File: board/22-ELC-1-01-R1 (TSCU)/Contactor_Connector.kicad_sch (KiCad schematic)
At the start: 18 parts, among them J10 Conn_02x02_Counter_Clockwise, J9 Conn_02x02_Counter_Clockwise, Q12 2N7002, Q13 CSD18540Q5B

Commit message: Ready for review
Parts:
- renumbered C27 to C6, C28 to C7, D8 to D5, J9 to J8, J10 to J9, Q12 to Q2, Q13 to Q3, R47 to R10, R48 to R11, R49 to R12, R50 to R13, R51 to R14, R43 to R7, R46 to R8, R36 to R9, TP15 to TP7, TP16 to TP8, TP17 to TP9
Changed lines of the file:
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@@
   (symbol (lib_id "power:GND") (at 74.93 120.65 0) (unit 1)
     (in_bom yes) (on_board yes)
-    (property "Reference" "#PWR093" (id 0) (at 74.93 127 0)
+    (property "Reference" "#PWR030" (id 0) (at 74.93 127 0)
       (effects (font (size 1.27 1.27)) hide)
     )
@@
   (symbol (lib_id "Device:R") (at 59.69 113.03 90) (unit 1)
     (in_bom yes) (on_board yes)
-    (property "Reference" "R43" (id 0) (at 58.5216 111.252 0)
+    (property "Reference" "R7" (id 0) (at 58.5216 111.252 0)
       (effects (font (size 1.27 1.27)) (justify left))
     )
@@
   (symbol (lib_id "Device:R") (at 80.01 106.68 270) (unit 1)
     (in_bom yes) (on_board yes)
-    (property "Reference" "R46" (id 0) (at 80.01 101.4222 90))
+    (property "Reference" "R8" (id 0) (at 80.01 101.4222 90))
     (property "Value" "100" (id 1) (at 80.01 103.7336 90))
     (property "Footprint" "Resistor_SMD:R_0603_1608Metric_Pad0.98x0.95mm_HandSolder" (id 2) (at 80.01 104.902 90)
@@
   (symbol (lib_id "Device:Q_NMOS_GSD") (at 72.39 113.03 0) (unit 1)
     (in_bom yes) (on_board yes)
-    (property "Reference" "Q12" (id 0) (at 77.6224 111.8616 0)
+    (property "Reference" "Q2" (id 0) (at 77.6224 111.8616 0)
       (effects (font (size 1.27 1.27)) (justify left))
     )
@@
   (symbol (lib_id "Device:R") (at 92.71 140.97 0) (unit 1)
     (in_bom yes) (on_board yes)
-    (property "Reference" "R47" (id 0) (at 94.488 139.8016 0)
+    (property "Reference" "R10" (id 0) (at 94.488 139.8016 0)
       (effects (font (size 1.27 1.27)) (justify left))
     )
@@
   (symbol (lib_id "Device:LED") (at 92.71 151.13 90) (unit 1)
     (in_bom yes) (on_board yes)
-    (property "Reference" "D8" (id 0) (at 95.7072 150.1394 90)
+    (property "Reference" "D5" (id 0) (at 95.7072 150.1394 90)
       (effects (font (size 1.27 1.27)) (justify right))
     )
@@
   (symbol (lib_id "power:GND") (at 92.71 154.94 0) (unit 1)
     (in_bom yes) (on_board yes)
-    (property "Reference" "#PWR094" (id 0) (at 92.71 161.29 0)
+    (property "Reference" "#PWR032" (id 0) (at 92.71 161.29 0)
       (effects (font (size 1.27 1.27)) hide)
     )
@@
   (symbol (lib_id "Device:R") (at 241.3 93.98 270) (unit 1)
     (in_bom yes) (on_board yes)
-    (property "Reference" "R51" (id 0) (at 241.3 88.7222 90))
+    (property "Reference" "R14" (id 0) (at 241.3 88.7222 90))
     (property "Value" "1k" (id 1) (at 241.3 91.0336 90))
     (property "Footprint" "Resistor_SMD:R_0603_1608Metric_Pad0.98x0.95mm_HandSolder" (id 2) (at 241.3 92.202 90)
@@
   (symbol (lib_id "power:+5V") (at 208.28 97.79 180) (unit 1)
     (in_bom yes) (on_board yes)
-    (property "Reference" "#PWR097" (id 0) (at 208.28 93.98 0)
+    (property "Reference" "#PWR035" (id 0) (at 208.28 93.98 0)
       (effects (font (size 1.27 1.27)) hide)
     )
@@
   (symbol (lib_id "power:+5V") (at 128.905 96.52 0) (unit 1)
     (in_bom yes) (on_board yes)
-    (property "Reference" "#PWR095" (id 0) (at 128.905 100.33 0)
+    (property "Reference" "#PWR033" (id 0) (at 128.905 100.33 0)
       (effects (font (size 1.27 1.27)) hide)
     )
@@
   (symbol (lib_id "Connector_Generic:Conn_02x02_Counter_Clockwise") (at 151.13 83.82 0) (unit 1)
     (in_bom yes) (on_board yes)
-    (property "Reference" "J9" (id 0) (at 152.4 81.28 0))
+    (property "Reference" "J8" (id 0) (at 152.4 81.28 0))
     (property "Value" "Conn_02x02_Counter_Clockwise" (id 1) (at 152.4 74.93 0)
       (effects (font (size 1.27 1.27)) hide)
@@
   (symbol (lib_id "Connector_Generic:Conn_02x02_Counter_Clockwise") (at 217.17 83.82 0) (unit 1)
     (in_bom yes) (on_board yes)
-    (property "Reference" "J10" (id 0) (at 218.44 81.28 0))
+    (property "Reference" "J9" (id 0) (at 218.44 81.28 0))
     (property "Value" "Conn_02x02_Counter_Clockwise" (id 1) (at 218.44 74.93 0)
       (effects (font (size 1.27 1.27)) hide)
@@
   (symbol (lib_id "Device:R") (at 234.95 97.79 0) (unit 1)
     (in_bom yes) (on_board yes)
-    (property "Reference" "R50" (id 0) (at 236.728 96.6216 0)
+    (property "Reference" "R13" (id 0) (at 236.728 96.6216 0)
       (effects (font (size 1.27 1.27)) (justify left))
     )
@@
   (symbol (lib_id "Device:R") (at 210.82 91.44 0) (unit 1)
     (in_bom yes) (on_board yes)
-    (property "Reference" "R49" (id 0) (at 212.598 90.2716 0)
+    (property "Reference" "R12" (id 0) (at 212.598 90.2716 0)
       (effects (font (size 1.27 1.27)) (justify left))
     )
@@
   (symbol (lib_id "power:GND") (at 146.05 83.82 270) (unit 1)
     (in_bom yes) (on_board yes)
-    (property "Reference" "#PWR096" (id 0) (at 139.7 83.82 0)
+    (property "Reference" "#PWR034" (id 0) (at 139.7 83.82 0)
       (effects (font (size 1.27 1.27)) hide)
     )
@@
   (symbol (lib_id "power:GND") (at 212.09 83.82 270) (unit 1)
     (in_bom yes) (on_board yes)
-    (property "Reference" "#PWR098" (id 0) (at 205.74 83.82 0)
+    (property "Reference" "#PWR036" (id 0) (at 205.74 83.82 0)
       (effects (font (size 1.27 1.27)) hide)
     )
@@
   (symbol (lib_id "Device:C_Small") (at 205.74 91.44 0) (mirror y) (unit 1)
     (in_bom yes) (on_board yes)
-    (property "Reference" "C28" (id 0) (at 200.66 90.17 0)
+    (property "Reference" "C7" (id 0) (at 200.66 90.17 0)
       (effects (font (size 1.27 1.27)) (justify right))
     )
@@
   (symbol (lib_id "Device:R") (at 144.78 91.44 0) (unit 1)
     (in_bom yes) (on_board yes)
-    (property "Reference" "R48" (id 0) (at 146.558 90.2716 0)
+    (property "Reference" "R11" (id 0) (at 146.558 90.2716 0)
       (effects (font (size 1.27 1.27)) (justify left))
     )
@@
   (symbol (lib_id "Device:C_Small") (at 139.7 91.44 0) (mirror y) (unit 1)
     (in_bom yes) (on_board yes)
-    (property "Reference" "C27" (id 0) (at 134.62 90.17 0)
+    (property "Reference" "C6" (id 0) (at 134.62 90.17 0)
       (effects (font (size 1.27 1.27)) (justify right))
     )
@@
   (symbol (lib_id "LHRE_Component_Library:CSD18512Q5B") (at 227.33 93.98 0) (mirror y) (unit 1)
     (in_bom yes) (on_board yes)
-    (property "Reference" "Q13" (id 0) (at 231.14 90.17 0)
+    (property "Reference" "Q3" (id 0) (at 231.14 90.17 0)
       (effects (font (size 1.27 1.27)) (justify left))
     )
@@
   (symbol (lib_id "Connector:TestPoint") (at 62.23 57.15 0) (unit 1)
     (in_bom yes) (on_board yes)
-    (property "Reference" "TP16" (id 0) (at 60.96 52.07 0)
+    (property "Reference" "TP8" (id 0) (at 60.96 52.07 0)
       (effects (font (size 1.27 1.27)) (justify left))
     )
@@
   (symbol (lib_id "Connector:TestPoint") (at 62.23 82.55 0) (unit 1)
     (in_bom yes) (on_board yes)
-    (property "Reference" "TP17" (id 0) (at 60.96 77.47 0)
+    (property "Reference" "TP9" (id 0) (at 60.96 77.47 0)
       (effects (font (size 1.27 1.27)) (justify left))
     )
@@
   (symbol (lib_id "Connector:TestPoint") (at 53.34 113.03 0) (unit 1)
     (in_bom yes) (on_board yes)
-    (property "Reference" "TP15" (id 0) (at 52.07 107.95 0)
+    (property "Reference" "TP7" (id 0) (at 52.07 107.95 0)
       (effects (font (size 1.27 1.27)) (justify left))
     )
@@
   (symbol (lib_id "power:+5V") (at 87.63 93.98 0) (unit 1)
     (in_bom yes) (on_board yes)
-    (property "Reference" "#PWR091" (id 0) (at 87.63 97.79 0)
+    (property "Reference" "#PWR031" (id 0) (at 87.63 97.79 0)
       (effects (font (size 1.27 1.27)) hide)
     )
@@
   (symbol (lib_id "Device:R") (at 87.63 97.79 0) (unit 1)
     (in_bom yes) (on_board yes)
-    (property "Reference" "R36" (id 0) (at 89.408 96.6216 0)
-      (effects (font (size 1.27 1.27)) (justify left))
-    )
+    (property "Reference" "R9" (id 0) (at 89.408 96.6216 0)
+      (effects (font (size 1.27 1.27)) (justify left))
+    )

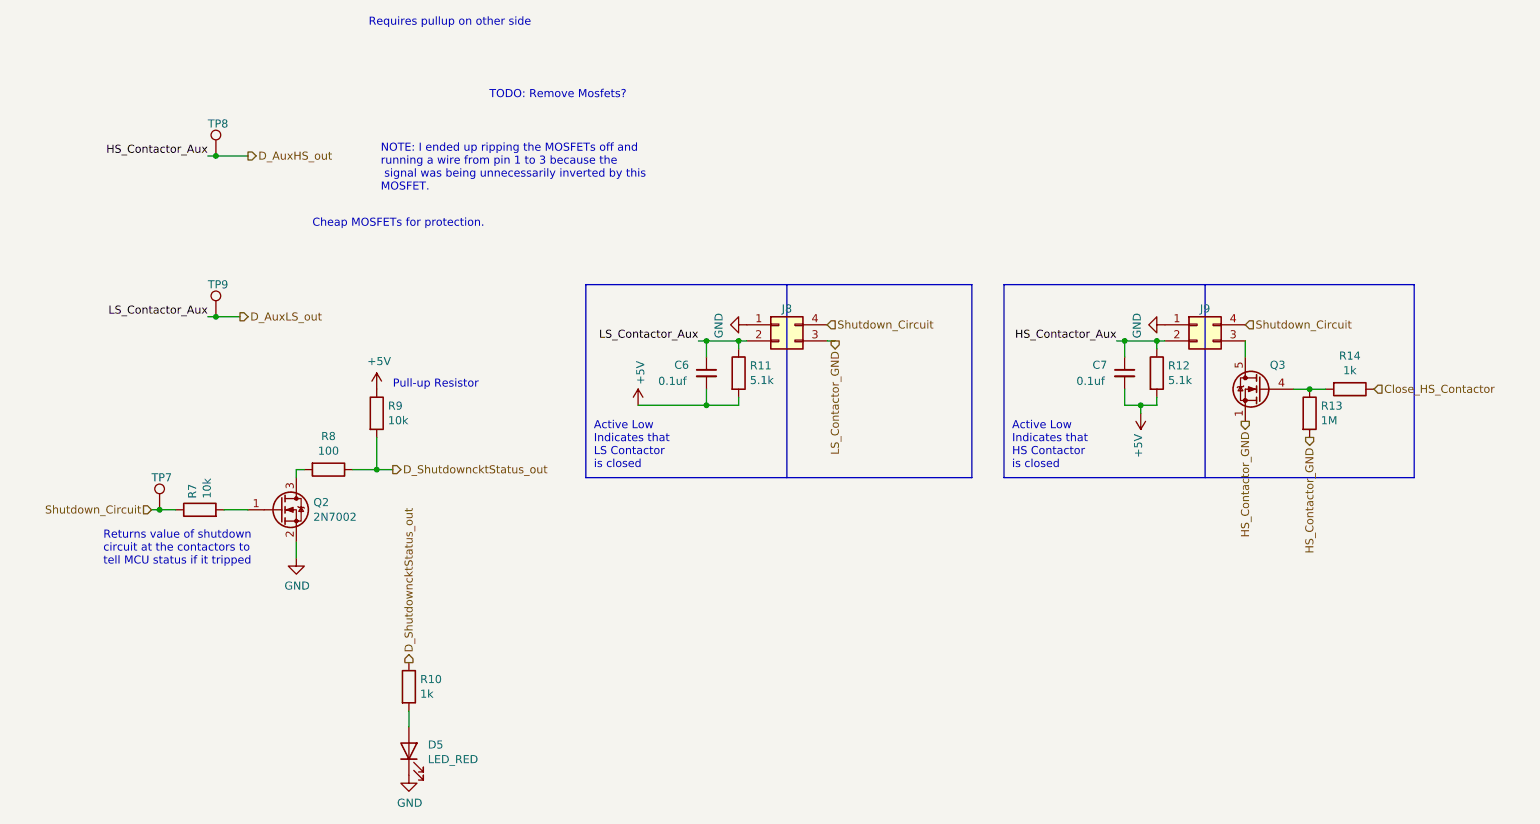
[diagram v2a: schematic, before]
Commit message: All good except need to switch everything to accepting 24v power
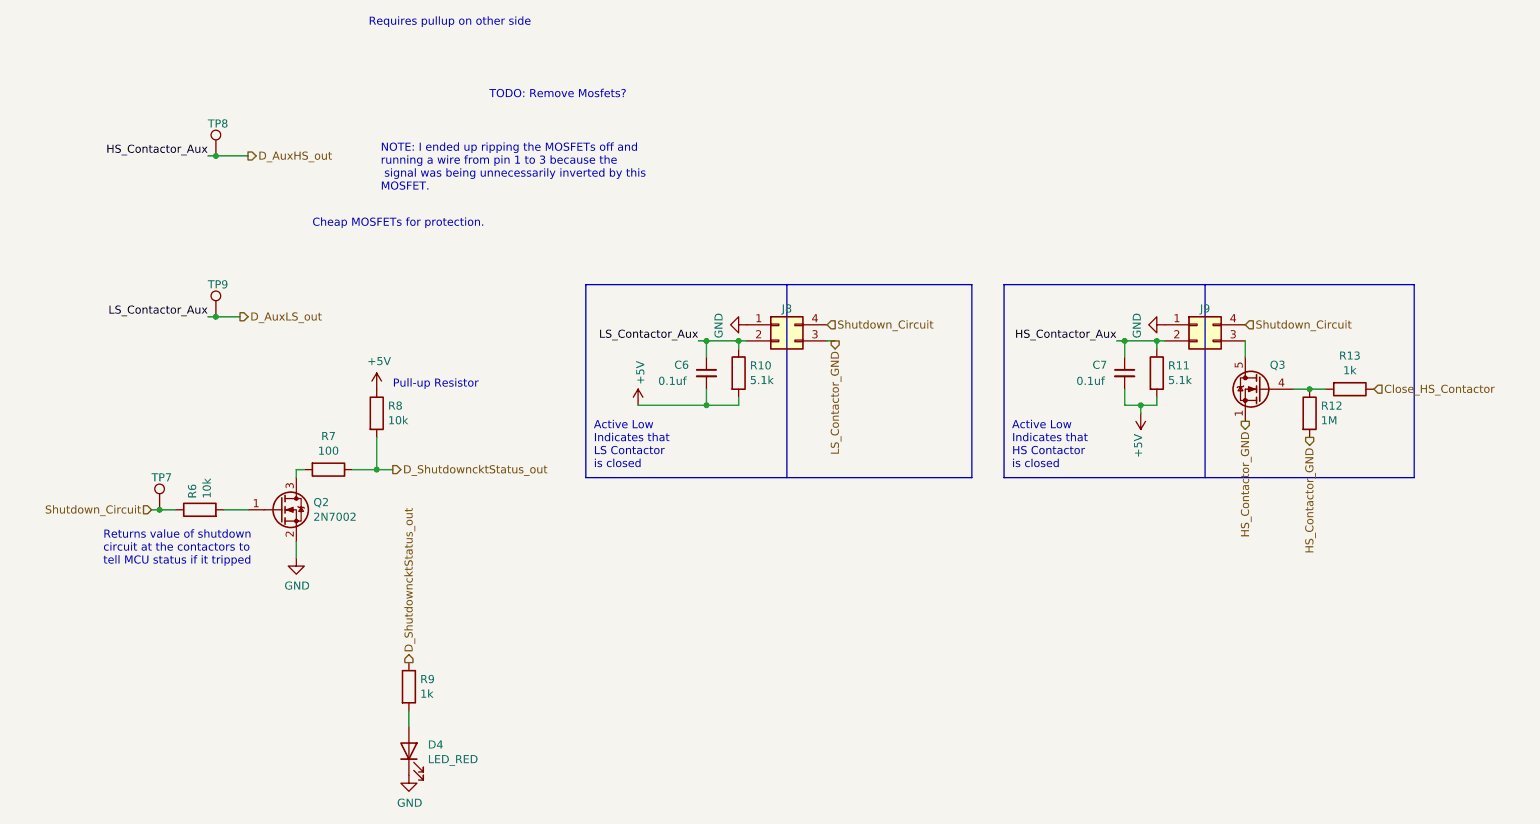
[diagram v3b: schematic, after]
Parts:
- renumbered D5 to D4, R11 to R10, R12 to R11, R13 to R12, R14 to R13, R7 to R6, R8 to R7, R9 to R8, R10 to R9
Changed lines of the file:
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@@
   (symbol (lib_id "power:GND") (at 74.93 120.65 0) (unit 1)
     (in_bom yes) (on_board yes)
-    (property "Reference" "#PWR030" (id 0) (at 74.93 127 0)
+    (property "Reference" "#PWR031" (id 0) (at 74.93 127 0)
       (effects (font (size 1.27 1.27)) hide)
     )
@@
   (symbol (lib_id "Device:R") (at 59.69 113.03 90) (unit 1)
     (in_bom yes) (on_board yes)
-    (property "Reference" "R7" (id 0) (at 58.5216 111.252 0)
+    (property "Reference" "R6" (id 0) (at 58.5216 111.252 0)
       (effects (font (size 1.27 1.27)) (justify left))
     )
@@
   (symbol (lib_id "Device:R") (at 80.01 106.68 270) (unit 1)
     (in_bom yes) (on_board yes)
-    (property "Reference" "R8" (id 0) (at 80.01 101.4222 90))
+    (property "Reference" "R7" (id 0) (at 80.01 101.4222 90))
     (property "Value" "100" (id 1) (at 80.01 103.7336 90))
     (property "Footprint" "Resistor_SMD:R_0603_1608Metric_Pad0.98x0.95mm_HandSolder" (id 2) (at 80.01 104.902 90)
@@
   (symbol (lib_id "Device:R") (at 92.71 140.97 0) (unit 1)
     (in_bom yes) (on_board yes)
-    (property "Reference" "R10" (id 0) (at 94.488 139.8016 0)
+    (property "Reference" "R9" (id 0) (at 94.488 139.8016 0)
       (effects (font (size 1.27 1.27)) (justify left))
     )
@@
   (symbol (lib_id "Device:LED") (at 92.71 151.13 90) (unit 1)
     (in_bom yes) (on_board yes)
-    (property "Reference" "D5" (id 0) (at 95.7072 150.1394 90)
+    (property "Reference" "D4" (id 0) (at 95.7072 150.1394 90)
       (effects (font (size 1.27 1.27)) (justify right))
     )
@@
   (symbol (lib_id "power:GND") (at 92.71 154.94 0) (unit 1)
     (in_bom yes) (on_board yes)
-    (property "Reference" "#PWR032" (id 0) (at 92.71 161.29 0)
+    (property "Reference" "#PWR033" (id 0) (at 92.71 161.29 0)
       (effects (font (size 1.27 1.27)) hide)
     )
@@
   (symbol (lib_id "Device:R") (at 241.3 93.98 270) (unit 1)
     (in_bom yes) (on_board yes)
-    (property "Reference" "R14" (id 0) (at 241.3 88.7222 90))
+    (property "Reference" "R13" (id 0) (at 241.3 88.7222 90))
     (property "Value" "1k" (id 1) (at 241.3 91.0336 90))
     (property "Footprint" "Resistor_SMD:R_0603_1608Metric_Pad0.98x0.95mm_HandSolder" (id 2) (at 241.3 92.202 90)
@@
   (symbol (lib_id "power:+5V") (at 208.28 97.79 180) (unit 1)
     (in_bom yes) (on_board yes)
-    (property "Reference" "#PWR035" (id 0) (at 208.28 93.98 0)
+    (property "Reference" "#PWR036" (id 0) (at 208.28 93.98 0)
       (effects (font (size 1.27 1.27)) hide)
     )
@@
   (symbol (lib_id "power:+5V") (at 128.905 96.52 0) (unit 1)
     (in_bom yes) (on_board yes)
-    (property "Reference" "#PWR033" (id 0) (at 128.905 100.33 0)
+    (property "Reference" "#PWR034" (id 0) (at 128.905 100.33 0)
       (effects (font (size 1.27 1.27)) hide)
     )
@@
   (symbol (lib_id "Device:R") (at 234.95 97.79 0) (unit 1)
     (in_bom yes) (on_board yes)
-    (property "Reference" "R13" (id 0) (at 236.728 96.6216 0)
+    (property "Reference" "R12" (id 0) (at 236.728 96.6216 0)
       (effects (font (size 1.27 1.27)) (justify left))
     )
@@
   (symbol (lib_id "Device:R") (at 210.82 91.44 0) (unit 1)
     (in_bom yes) (on_board yes)
-    (property "Reference" "R12" (id 0) (at 212.598 90.2716 0)
+    (property "Reference" "R11" (id 0) (at 212.598 90.2716 0)
       (effects (font (size 1.27 1.27)) (justify left))
     )
@@
   (symbol (lib_id "power:GND") (at 146.05 83.82 270) (unit 1)
     (in_bom yes) (on_board yes)
-    (property "Reference" "#PWR034" (id 0) (at 139.7 83.82 0)
+    (property "Reference" "#PWR035" (id 0) (at 139.7 83.82 0)
       (effects (font (size 1.27 1.27)) hide)
     )
@@
   (symbol (lib_id "power:GND") (at 212.09 83.82 270) (unit 1)
     (in_bom yes) (on_board yes)
-    (property "Reference" "#PWR036" (id 0) (at 205.74 83.82 0)
+    (property "Reference" "#PWR037" (id 0) (at 205.74 83.82 0)
       (effects (font (size 1.27 1.27)) hide)
     )
@@
   (symbol (lib_id "Device:R") (at 144.78 91.44 0) (unit 1)
     (in_bom yes) (on_board yes)
-    (property "Reference" "R11" (id 0) (at 146.558 90.2716 0)
+    (property "Reference" "R10" (id 0) (at 146.558 90.2716 0)
       (effects (font (size 1.27 1.27)) (justify left))
     )
@@
   (symbol (lib_id "power:+5V") (at 87.63 93.98 0) (unit 1)
     (in_bom yes) (on_board yes)
-    (property "Reference" "#PWR031" (id 0) (at 87.63 97.79 0)
+    (property "Reference" "#PWR032" (id 0) (at 87.63 97.79 0)
       (effects (font (size 1.27 1.27)) hide)
     )
@@
   (symbol (lib_id "Device:R") (at 87.63 97.79 0) (unit 1)
     (in_bom yes) (on_board yes)
-    (property "Reference" "R9" (id 0) (at 89.408 96.6216 0)
-      (effects (font (size 1.27 1.27)) (justify left))
-    )
+    (property "Reference" "R8" (id 0) (at 89.408 96.6216 0)
+      (effects (font (size 1.27 1.27)) (justify left))
+    )
